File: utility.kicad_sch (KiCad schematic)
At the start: 16 parts, among them J10 Conn_01x02, J3 Conn_01x02, J4 Conn_01x01, J5 Conn_01x04, J6 Conn_01x06, J7 Conn_01x02, J8 Conn_01x03, J9 Conn_01x03, P1 TYPE_C Receptacle, U8 TJA1051T

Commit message: LATEST UPDATES
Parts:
- removed J4: Conn_01x01, Connector_PinSocket_1.27mm:PinSocket_1x01_P1.27mm_Vertical, symbol Connector_Generic:Conn_01x01
- added J4: Conn_01x02, Connector_PinSocket_2.00mm:PinSocket_1x02_P2.00mm_Vertical, symbol Connector_Generic:Conn_01x02
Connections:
- net GND: now also J4.1 (Pin_1); no longer R50.2
- new net TEMP_SENSOR: J4.2 (Pin_2), R50.2
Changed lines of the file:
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@@
+	)
+	(junction
+		(at 124.46 36.83)
+		(diameter 0)
+		(color 0 0 0 0)
 	)
 	(junction
@@
 		(color 0 0 0 0)
 	)
-	(junction
-		(at 124.46 36.83)
-		(diameter 0)
-		(color 0 0 0 0)
-	)
 	(no_connect
 		(at 210.82 45.72)
@@
 		(pts
 			(xy 41.91 26.67) (xy 41.91 31.75)
-		)
-		(stroke
-			(width 0)
-			(type default)
-		)
-	)
-	(wire
-		(pts
-			(xy 124.46 36.83) (xy 129.54 36.83)
 		)
 		(stroke
@@
 	(symbol
 		(lib_id "power:GND")
-		(at 129.54 36.83 180)
+		(at 127 36.83 90)
 		(unit 1)
 		(exclude_from_sim no)
@@
 		(fields_autoplaced yes)
 		(property "Reference" "#PWR069"
-			(at 129.54 30.48 0)
+			(at 133.35 36.83 0)
 			(effects
 				(font
@@
 		)
 		(property "Value" "GND"
-			(at 129.54 31.75 0)
-			(effects
-				(font
-					(size 1.27 1.27)
-				)
+			(at 130.81 36.8299 90)
+			(effects
+				(font
+					(size 1.27 1.27)
+				)
+				(justify right)
 			)
 		)
 		(property "Footprint" ""
-			(at 129.54 36.83 0)
+			(at 127 36.83 0)
 			(effects
 				(font
@@
 		)
 		(property "Datasheet" ""
-			(at 129.54 36.83 0)
+			(at 127 36.83 0)
 			(effects
 				(font
@@
 		)
 		(property "Description" "Power symbol creates a global label with name \"GND\" , ground"
-			(at 129.54 36.83 0)
+			(at 127 36.83 0)
 			(effects
 				(font
@@
 	)
 	(symbol
+		(lib_id "Connector_Generic:Conn_01x02")
+		(at 127 41.91 270)
+		(unit 1)
+		(exclude_from_sim no)
+		(in_bom yes)
+		(on_board yes)
+		(dnp no)
+		(fields_autoplaced yes)
+		(property "Reference" "J4"
+			(at 129.54 40.6399 90)
+			(effects
+				(font
+					(size 1.27 1.27)
+				)
+				(justify left)
+			)
+		)
+		(property "Value" "Conn_01x02"
+			(at 129.54 43.1799 90)
+			(effects
+				(font
+					(size 1.27 1.27)
+				)
+				(justify left)
+			)
+		)
+		(property "Footprint" "Connector_PinSocket_2.00mm:PinSocket_1x02_P2.00mm_Vertical"
+			(at 127 41.91 0)
+			(effects
+				(font
+					(size 1.27 1.27)
+				)
+				(hide yes)
+			)
+		)
+		(property "Datasheet" "~"
+			(at 127 41.91 0)
+			(effects
+				(font
+					(size 1.27 1.27)
+				)
+				(hide yes)
+			)
+		)
+		(property "Description" "Generic connector, single row, 01x02, script generated (kicad-library-utils/schlib/autogen/connector/)"
+			(at 127 41.91 0)
+			(effects
+				(font
+					(size 1.27 1.27)
+				)
+				(hide yes)
+			)
+		)
+		(pin "1"
+		)
+		(pin "2"
+		)
+		(instances
+			(project ""
+				(path "/63ef3b9c-05f1-4b00-812a-fede2372efc7/47456917-9d2b-40cb-8a9e-ce53d71da470"
+					(reference "J4")
+					(unit 1)
+				)
+			)
+		)
+	)
+	(symbol
 		(lib_id "Device:R")
 		(at 264.16 49.53 180)
@@
 					(unit 1)
 				)
-			)
-		)
-	)
-	(symbol
-		(lib_id "Connector_Generic:Conn_01x01")
-		(at 124.46 41.91 270)
-		(unit 1)
-		(exclude_from_sim no)
-		(in_bom yes)
-		(on_board yes)
-		(dnp no)
-		(fields_autoplaced yes)
-		(property "Reference" "J4"
-			(at 127 40.6399 90)
-			(effects
-				(font
-					(size 1.27 1.27)
-				)
-				(justify left)
-			)
-		)
-		(property "Value" "Conn_01x01"
-			(at 127 43.1799 90)
-			(effects
-				(font
-					(size 1.27 1.27)
-				)
-				(justify left)
-			)
-		)
-		(property "Footprint" "Connector_PinSocket_1.27mm:PinSocket_1x01_P1.27mm_Vertical"
-			(at 124.46 41.91 0)
-			(effects
-				(font
-					(size 1.27 1.27)
-				)
-				(hide yes)
-			)
-		)
-		(property "Datasheet" "~"
-			(at 124.46 41.91 0)
-			(effects
-				(font
-					(size 1.27 1.27)
-				)
-				(hide yes)
-			)
-		)
-		(property "Description" "Generic connector, single row, 01x01, script generated (kicad-library-utils/schlib/autogen/connector/)"
-			(at 124.46 41.91 0)
-			(effects
-				(font
-					(size 1.27 1.27)
-				)
-				(hide yes)
-			)
-		)
-		(pin "1"
-		)
-		(instances
-			(project ""
-				(path "/63ef3b9c-05f1-4b00-812a-fede2372efc7/47456917-9d2b-40cb-8a9e-ce53d71da470"
-					(reference "J4")
-					(unit 1)
-				)

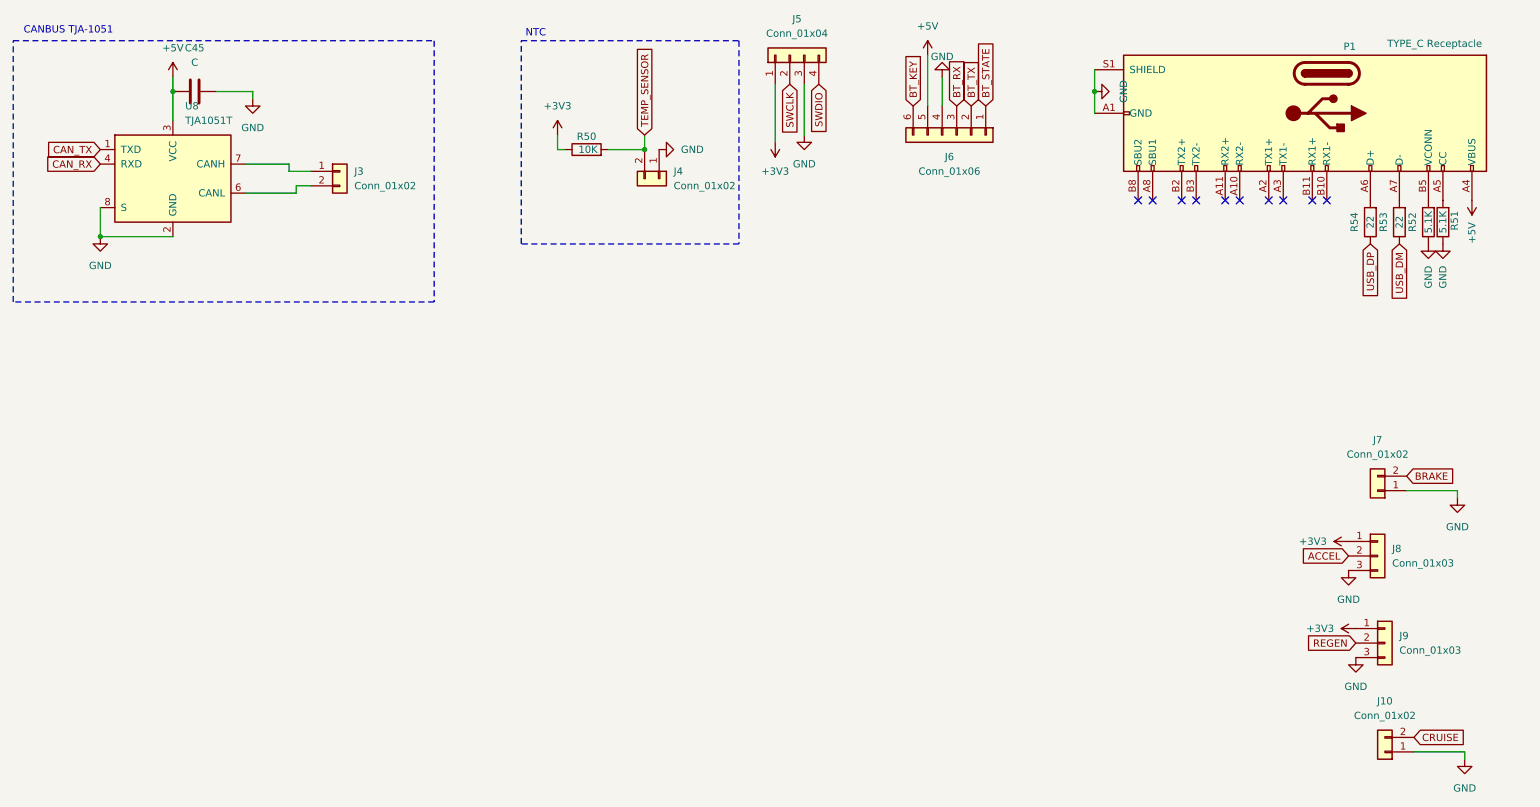
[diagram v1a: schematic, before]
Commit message: Fet Drivers  olarak IRS21867S, MOSFET olarak IAUS300N08S5N014 değiştirildi. Decoupler kısmı değiştirildi, (paraziter direnci arttırıldı.) buzzer düzeltildi ve utility kısmına alındı. CAN-BUS bitti. LDO sayısı 2x oldu
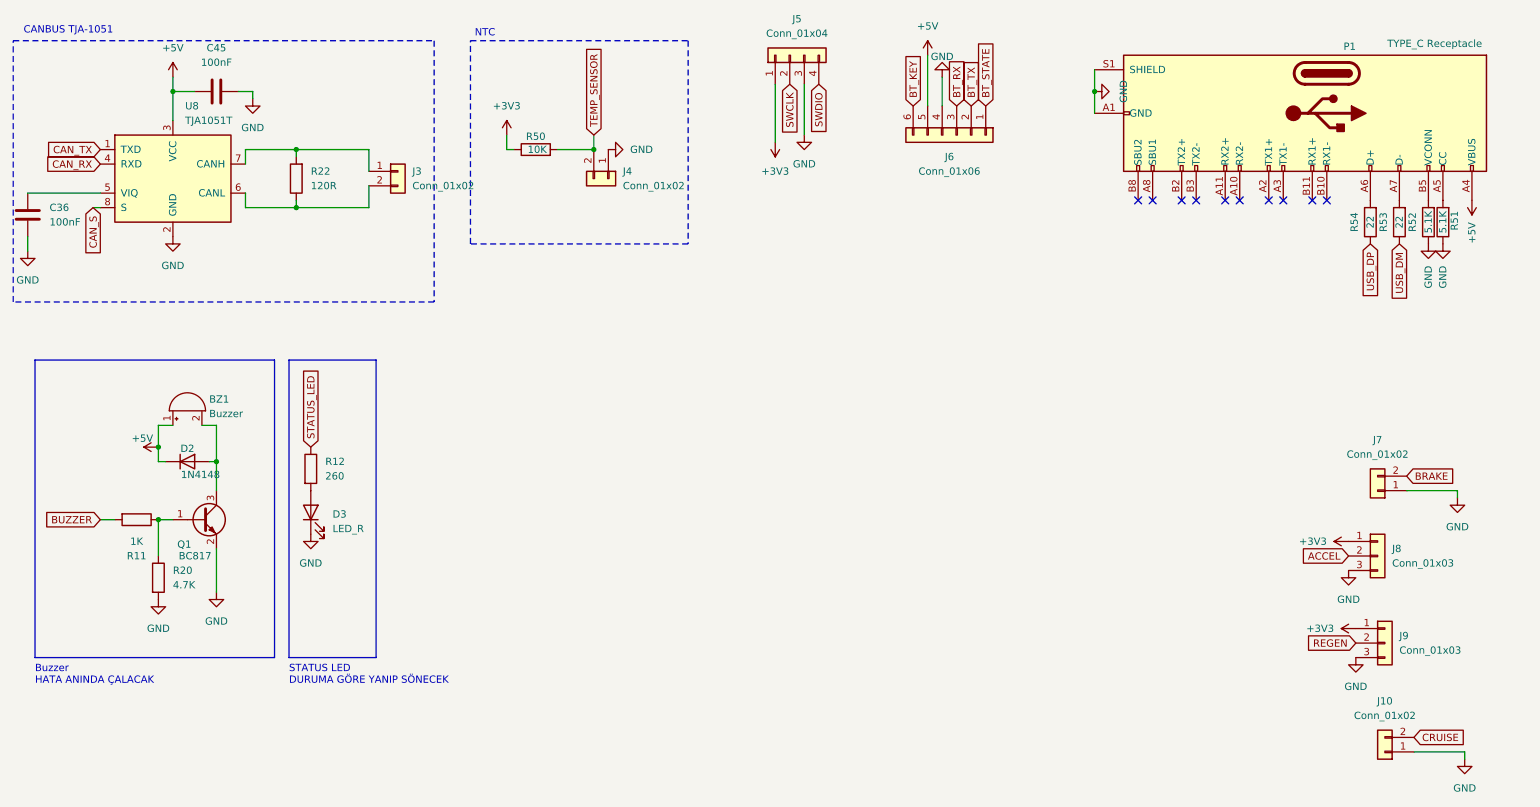
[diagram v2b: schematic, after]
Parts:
- added BZ1: Buzzer, Buzzer_Beeper:Buzzer_12x9.5RM7.6, symbol Device:Buzzer
- added C36: 100nF, symbol Device:C
- added D2: 1N4148, Diode_THT:D_DO-35_SOD27_P7.62mm_Horizontal, symbol Diode:1N4148
- added D3: LED_R, LED_THT:LED_D1.8mm_W3.3mm_H2.4mm, symbol Device:LED
- added Q1: BC817, Package_TO_SOT_SMD:SOT-23, symbol Transistor_BJT:BC817
- added R11: 1K, Resistor_THT:R_Axial_DIN0207_L6.3mm_D2.5mm_P7.62mm_Horizontal, symbol Device:R
- added R12: 260, Resistor_THT:R_Axial_DIN0207_L6.3mm_D2.5mm_P7.62mm_Horizontal, symbol Device:R
- added R20: 4.7K, Resistor_THT:R_Axial_DIN0207_L6.3mm_D2.5mm_P7.62mm_Horizontal, symbol Device:R
- added R22: 120R, symbol Device:R
- C45: value C -> 100nF
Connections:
- net +5V: now also BZ1.1 (+), D2.1 (K)
- net GND: now also C36.2, D3.1 (K), Q1.2 (E), R20.2; no longer U8.8 (S)
- net at U8.5 (VIQ): now also C36.1
- net at J3.2 (Pin_2), U8.6 (CANL): now also R22.1
- net at J3.1 (Pin_1), U8.7 (CANH): now also R22.2
- new net: BZ1.2 (-), D2.2 (A), Q1.3 (C)
- new net: D3.2 (A), R12.2
- new net: Q1.1 (B), R11.1, R20.1
- new net BUZZER: R11.2
- new net CAN_S: U8.8 (S)
- new net STATUS_LED: R12.1
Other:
- note added: "Buzzer HATA ANINDA ÇALACAK"
- note added: "STATUS LED DURUMA GÖRE YANIP SÖNECEK"
- moved on the sheet: C45, J3, J4, R50

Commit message: update Current sense
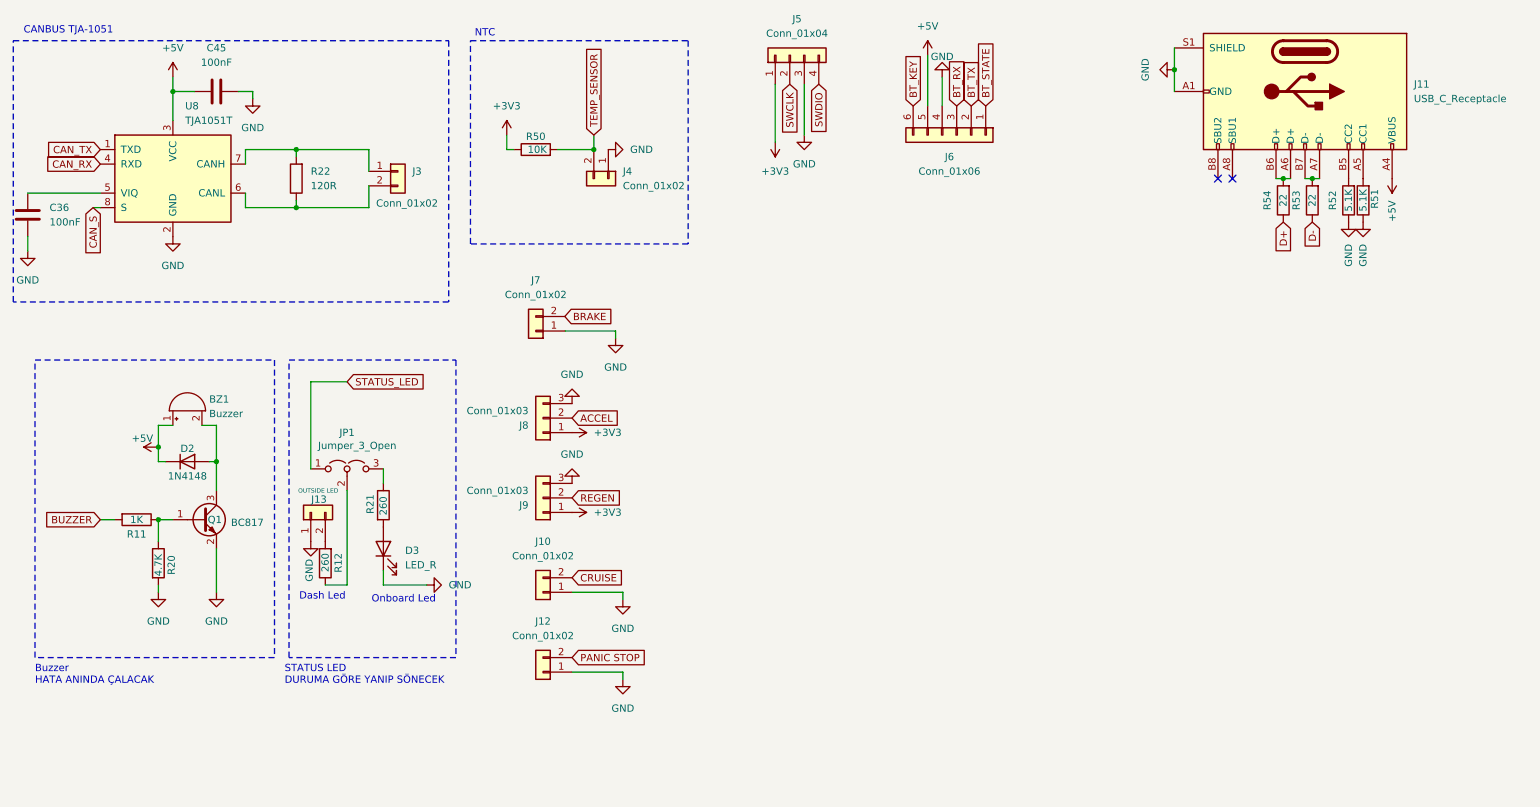
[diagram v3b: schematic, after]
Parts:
- removed P1: TYPE_C Receptacle, Connector_USB:USB_C_Receptacle_HRO_TYPE-C-31-M-12, symbol Connector:USB_C_Plug
- added J11: USB_C_Receptacle, Connector_USB:USB_C_Receptacle_GCT_USB4105-xx-A_16P_TopMnt_Horizontal, symbol Connector:USB_C_Receptacle_USB2.0_16P
- added J12: Conn_01x02, Connector_PinSocket_2.00mm:PinSocket_1x02_P2.00mm_Horizontal, symbol Connector_Generic:Conn_01x02
- added J13: OUTSIDE LED, Connector_PinSocket_2.00mm:PinSocket_1x02_P2.00mm_Horizontal, symbol Connector_Generic:Conn_01x02
- added JP1: Jumper_3_Open, Connector_PinHeader_1.27mm:PinHeader_1x03_P1.27mm_Horizontal, symbol Jumper:Jumper_3_Open
- added R21: 260, Resistor_SMD:R_0603_1608Metric_Pad0.98x0.95mm_HandSolder, symbol Device:R
- C36: footprint (none) -> Capacitor_SMD:C_0603_1608Metric_Pad1.08x0.95mm_HandSolder
- R22: footprint (none) -> Resistor_SMD:R_0603_1608Metric_Pad0.98x0.95mm_HandSolder
- R51, R52, R53, R54: footprint Resistor_THT:R_Axial_DIN0207_L6.3mm_D2.5mm_P7.62mm_Horizontal -> Resistor_SMD:R_0603_1608Metric_Pad0.98x0.95mm_HandSolder
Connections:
- net +5V: now also J11.A4 (VBUS), J11.A9 (VBUS), J11.B4 (VBUS), J11.B9 (VBUS)
- net GND: now also J11.A1 (GND), J11.A12 (GND), J11.B1 (GND), J11.B12 (GND), J11.S1 (SHIELD), J12.1 (Pin_1), J13.1 (Pin_1)
- net STATUS_LED: now also JP1.1 (A); no longer R12.1
- net at D3.2 (A): now also R21.2; no longer R12.2
- net at R53.2: now also J11.A7 (D-), J11.B7 (D-)
- net at R54.2: now also J11.A6 (D+), J11.B6 (D+)
- net at R51.2: now also J11.A5 (CC1)
- net at R52.2: now also J11.B5 (CC2)
- net USB_DM renamed D-
- net USB_DP renamed D+
- new net: JP1.2 (C), R12.1
- new net: J13.2 (Pin_2), R12.2
- new net: JP1.3 (B), R21.1
- new net PANIC STOP: J12.2 (Pin_2)
- no-connect marks 10 -> 2
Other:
- note added: "Dash Led"
- note added: "Onboard Led"
- moved on the sheet: D3, J10, J7, J8, J9, R12, R20, R51, R52, R53, R54

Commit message: LAST I HOPE
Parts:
- C45: footprint Capacitor_THT:C_Axial_L17.0mm_D7.0mm_P25.00mm_Horizontal -> Capacitor_SMD:C_1210_3225Metric_Pad1.33x2.70mm_HandSolder
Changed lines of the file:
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@@
 			)
 		)
-		(property "Footprint" "Capacitor_THT:C_Axial_L17.0mm_D7.0mm_P25.00mm_Horizontal"
+		(property "Footprint" "Capacitor_SMD:C_1210_3225Metric_Pad1.33x2.70mm_HandSolder"
 			(at 53.34 25.7048 0)
 			(effects

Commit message: bit artık
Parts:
- removed J10: Conn_01x02, Connector_PinSocket_2.00mm:PinSocket_1x02_P2.00mm_Horizontal, symbol Connector_Generic:Conn_01x02
- added Q2: BC817, Package_TO_SOT_SMD:SOT-23, symbol Transistor_BJT:BC817
- added R73: 470, Resistor_SMD:R_0603_1608Metric_Pad0.98x0.95mm_HandSolder, symbol Device:R
- JP1: footprint Connector_PinHeader_1.27mm:PinHeader_1x03_P1.27mm_Horizontal -> Connector_PinHeader_1.27mm:PinHeader_1x03_P1.27mm_Vertical
- R12: footprint Resistor_THT:R_Axial_DIN0207_L6.3mm_D2.5mm_P7.62mm_Horizontal -> Resistor_SMD:R_0603_1608Metric
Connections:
- net CAN_S is gone; now on net GND: U8.8 (S)
- net +5V: now also Q2.3 (C)
- net STATUS_LED: now also R73.2; no longer JP1.1 (A)
- net at R22.1, U8.6 (CANL): now also J3.1 (Pin_1); no longer J3.2 (Pin_2)
- net at R22.2, U8.7 (CANH): now also J3.2 (Pin_2); no longer J3.1 (Pin_1)
- new net: Q2.1 (B), R73.1
- new net: JP1.1 (A), Q2.2 (E)
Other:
- moved on the sheet: J12

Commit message: rev3
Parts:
- removed J6: Conn_01x06, Connector_PinSocket_1.27mm:PinSocket_1x06_P1.27mm_Vertical, symbol Connector_Generic:Conn_01x06
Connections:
- net at R12.1: now also JP1.3 (B); no longer JP1.2 (C)
- net at JP1.1 (A): now also R21.1; no longer Q2.2 (E)
- new net: JP1.2 (C), Q2.2 (E)
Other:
- moved on the sheet: JP1
